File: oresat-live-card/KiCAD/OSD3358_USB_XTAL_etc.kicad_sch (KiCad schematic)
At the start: 81 parts, among them J10 SM06B-SRSS-TB(LF)(SN), J2 SM06B-SRSS-TB(LF)(SN), U1 RCLAMP0504FB, U2 TUSB4020BI, U20 TPS2041BQDBVRQ1, U7 OSD3358-512M-BSM, U9 TPS2041BQDBVRQ1, Y1 24MHz, Y2 ABS07-32.768KHZ-T, Y3 24MHz

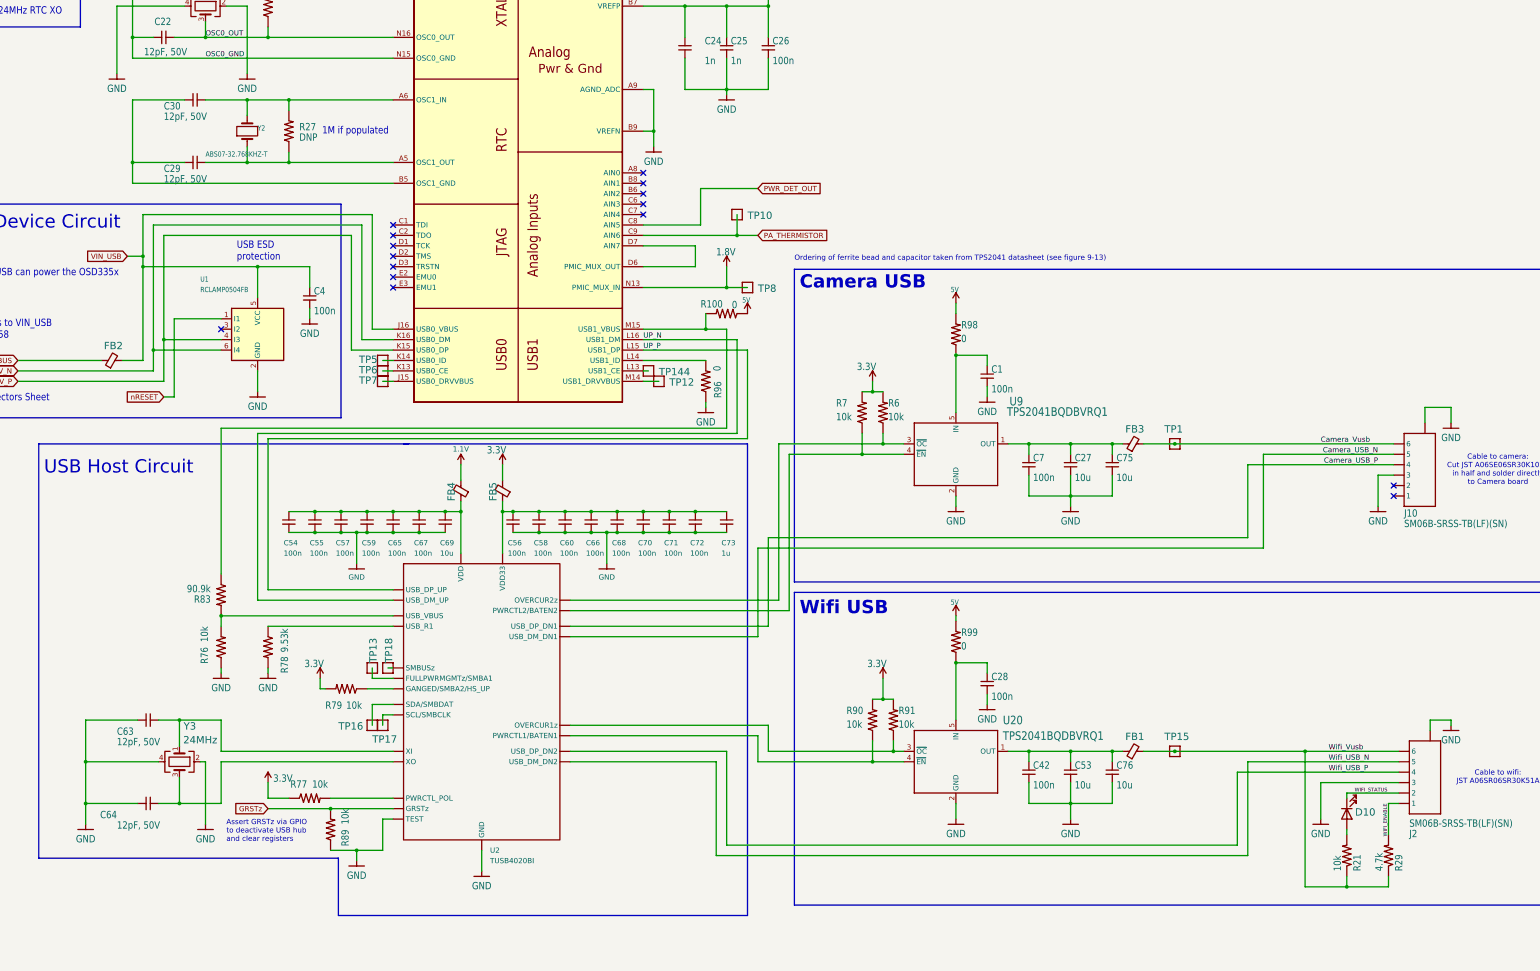
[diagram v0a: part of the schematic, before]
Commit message: completed tx/rx switch circuit and cleaned up GND references
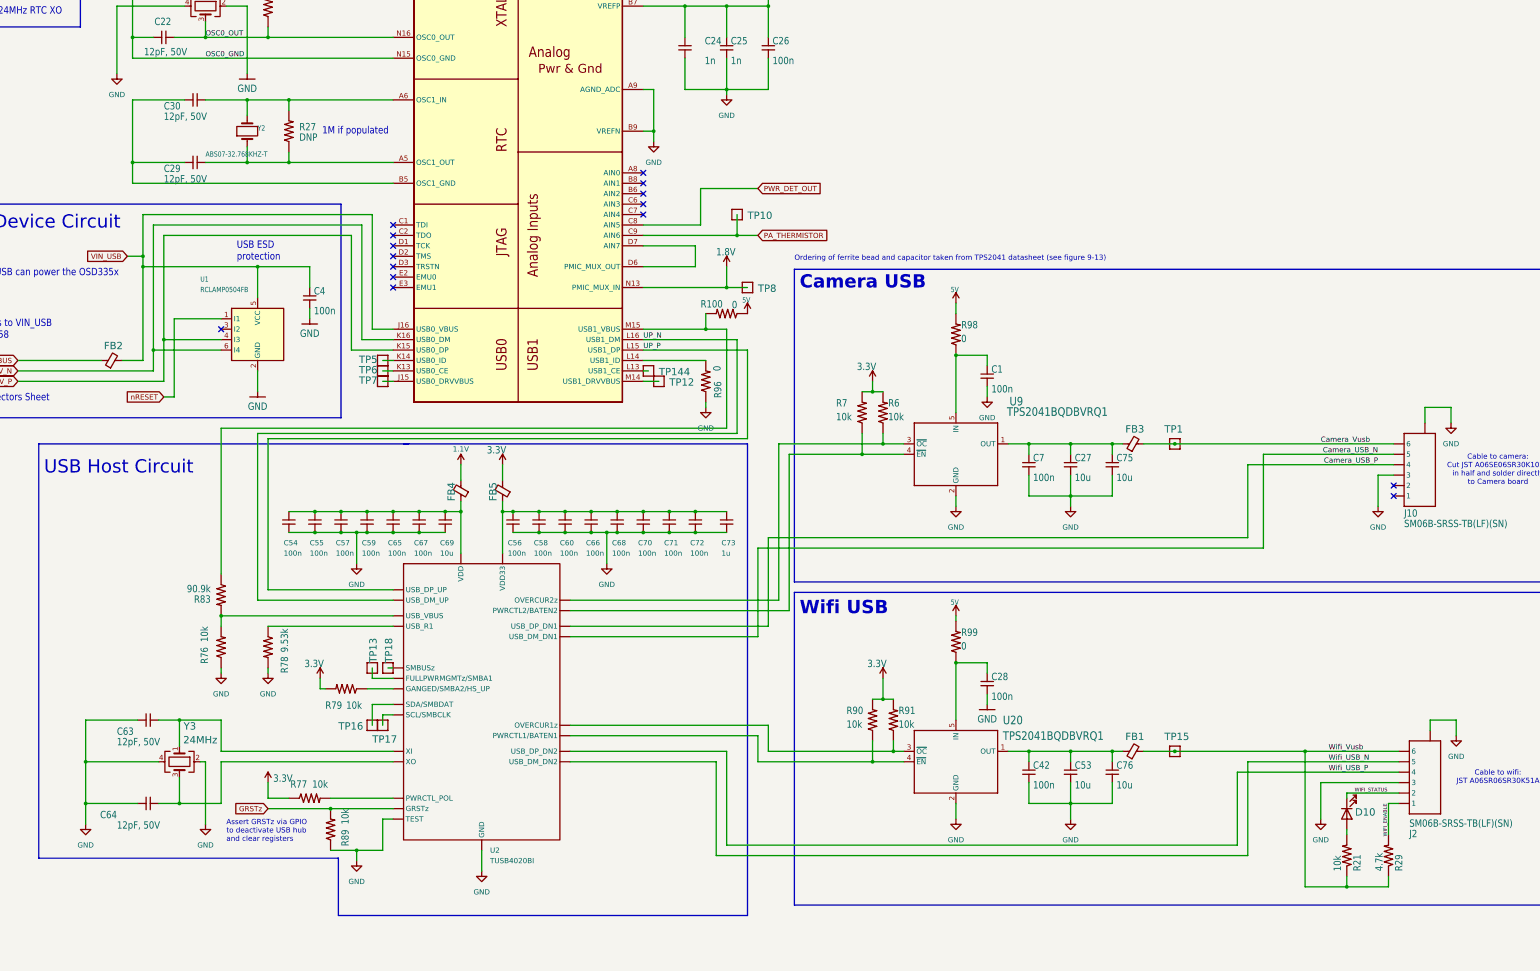
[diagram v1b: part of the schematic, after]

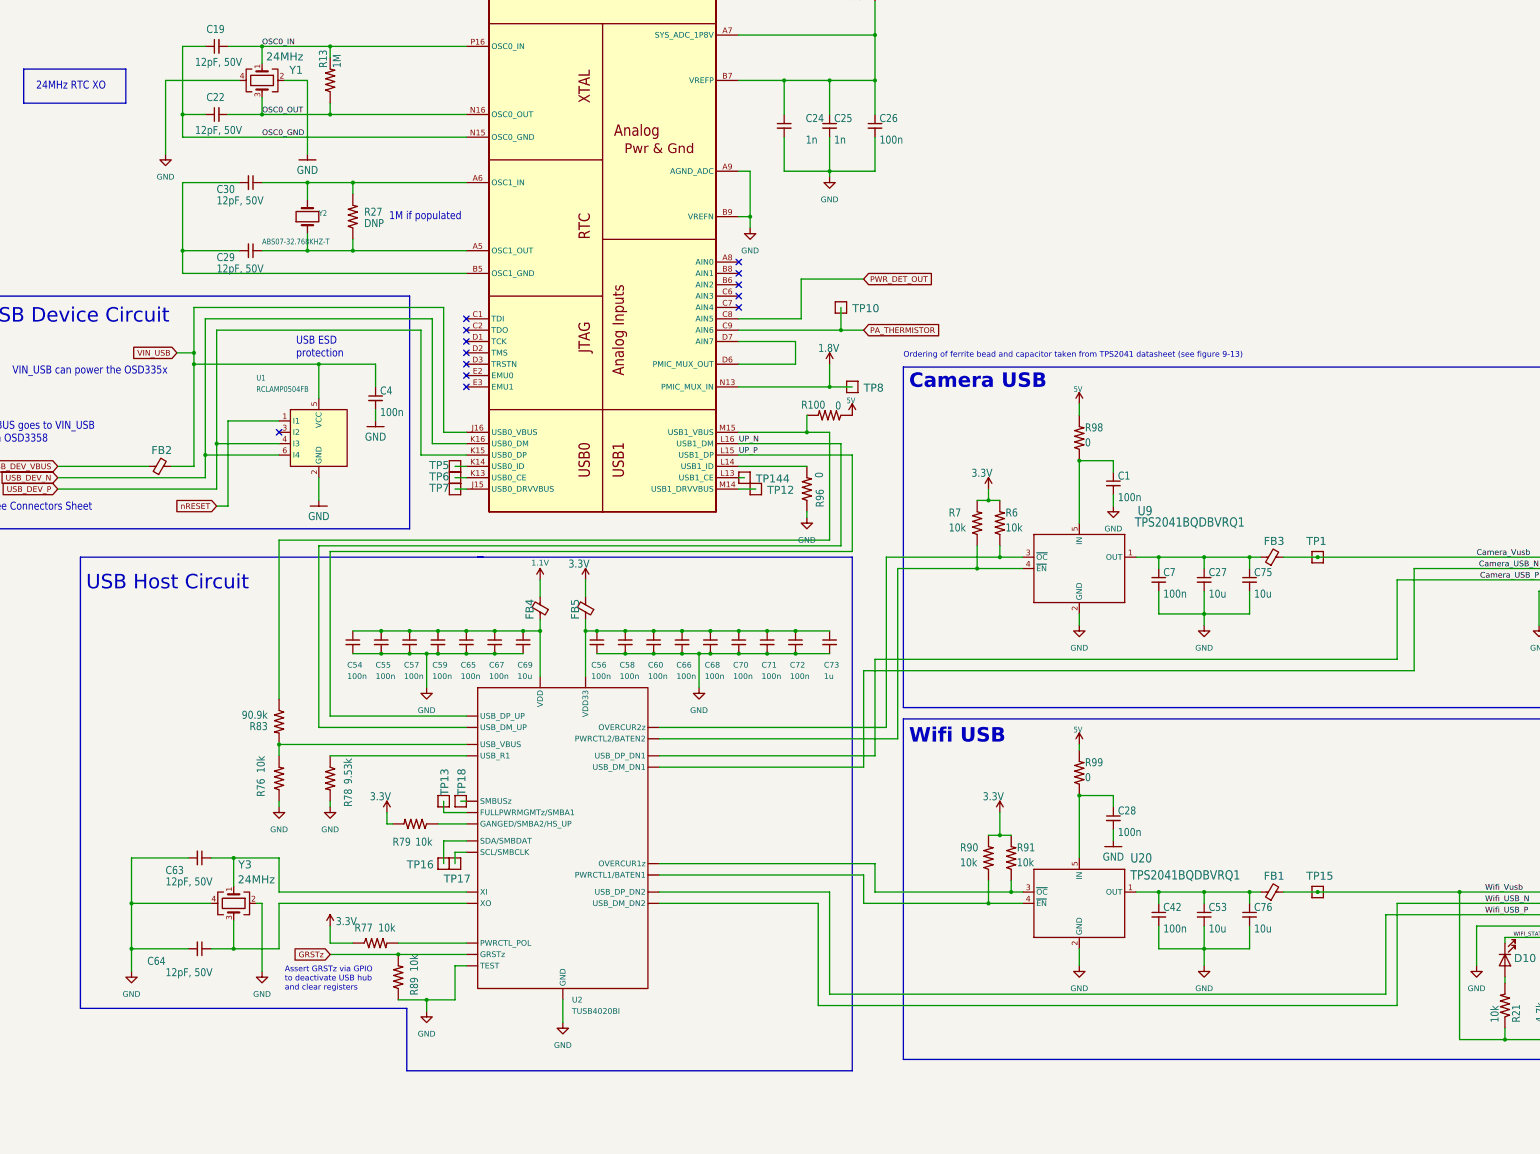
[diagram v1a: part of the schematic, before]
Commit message: completed LNA minus pwr detect.
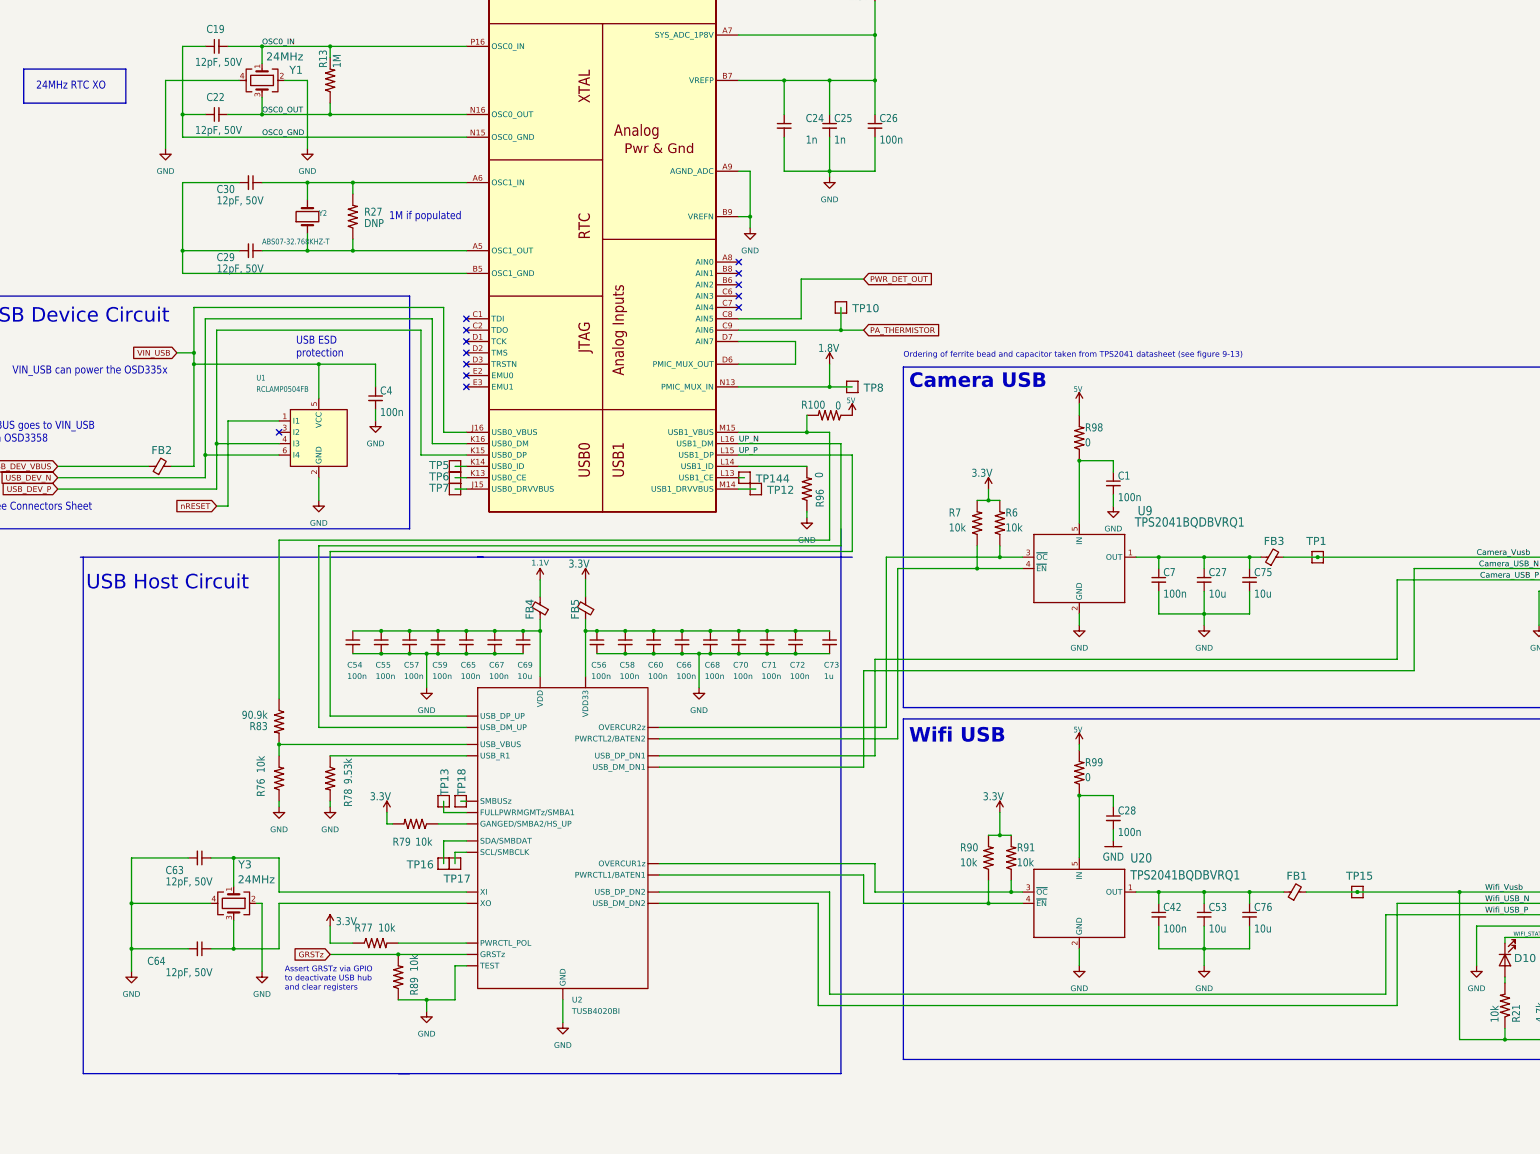
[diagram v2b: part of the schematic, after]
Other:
- moved on the sheet: FB1, TP15
